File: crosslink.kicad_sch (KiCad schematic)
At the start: 1 part

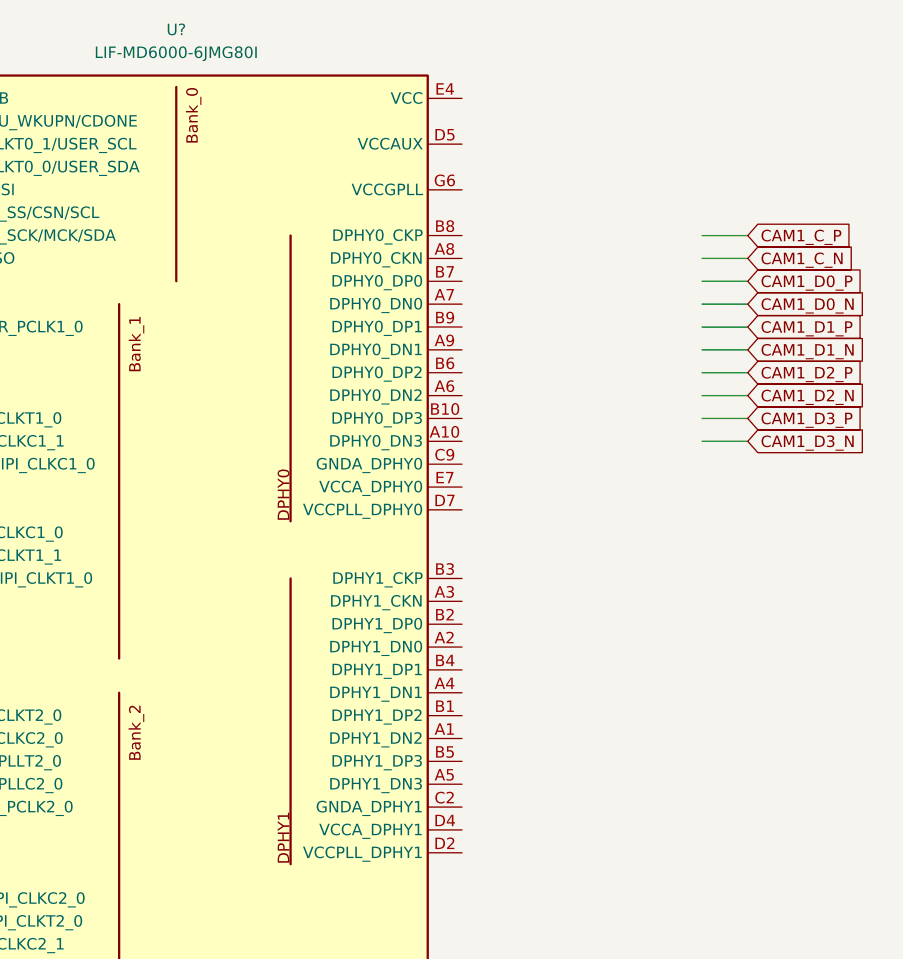
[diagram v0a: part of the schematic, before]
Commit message: [#52579] Connect CSI and DSI to CrossLink
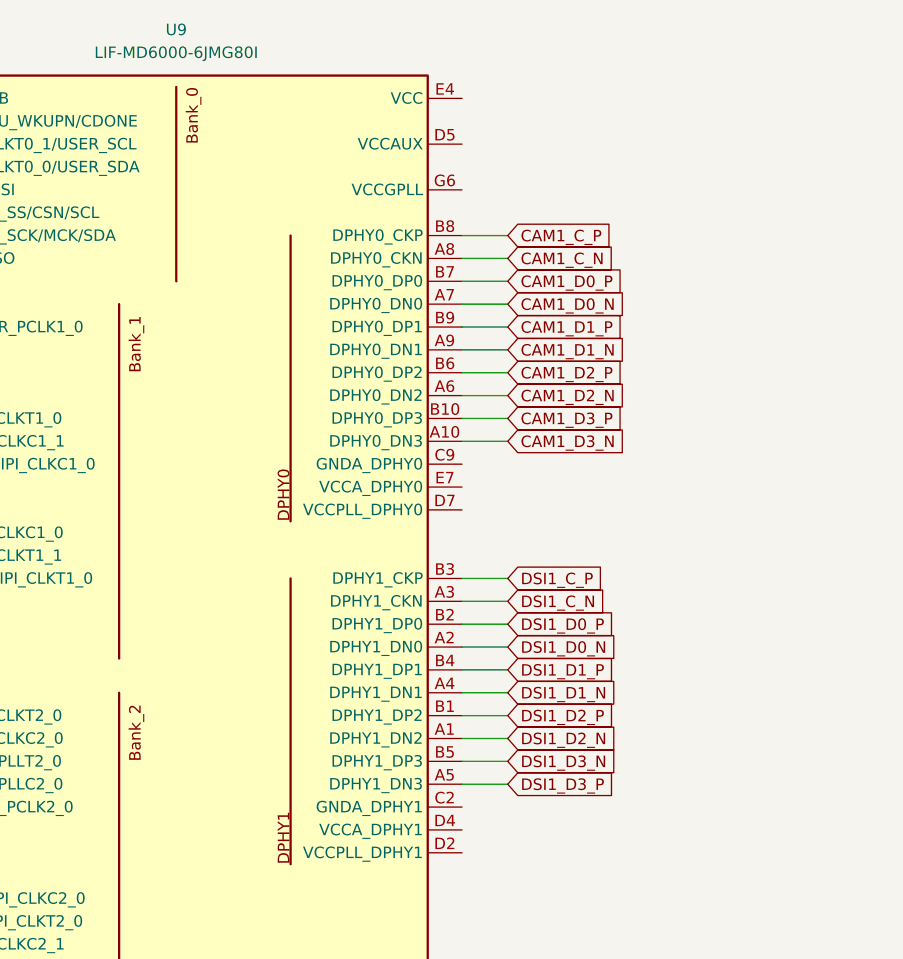
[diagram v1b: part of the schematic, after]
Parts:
- gave numbers to parts that had none: 1
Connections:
- net CAM1_C_N: now also U9.A8 (DPHY0_CKN)
- net CAM1_C_P: now also U9.B8 (DPHY0_CKP)
- net CAM1_D0_N: now also U9.A7 (DPHY0_DN0)
- net CAM1_D0_P: now also U9.B7 (DPHY0_DP0)
- net CAM1_D1_N: now also U9.A9 (DPHY0_DN1)
- net CAM1_D1_P: now also U9.B9 (DPHY0_DP1)
- net CAM1_D2_N: now also U9.A6 (DPHY0_DN2)
- net CAM1_D2_P: now also U9.B6 (DPHY0_DP2)
- net CAM1_D3_N: now also U9.A10 (DPHY0_DN3)
- net CAM1_D3_P: now also U9.B10 (DPHY0_DP3)
- net DSI1_D2_N: now reaches U9.A1 (DPHY1_DN2)
- net DSI1_D0_N: now reaches U9.A2 (DPHY1_DN0)
- net DSI1_C_N: now reaches U9.A3 (DPHY1_CKN)
- net DSI1_D1_N: now reaches U9.A4 (DPHY1_DN1)
- net DSI1_D3_P: now reaches U9.A5 (DPHY1_DN3)
- net DSI1_D2_P: now reaches U9.B1 (DPHY1_DP2)
- net DSI1_D0_P: now reaches U9.B2 (DPHY1_DP0)
- net DSI1_C_P: now reaches U9.B3 (DPHY1_CKP)
- net DSI1_D1_P: now reaches U9.B4 (DPHY1_DP1)
- net DSI1_D3_N: now reaches U9.B5 (DPHY1_DP3)

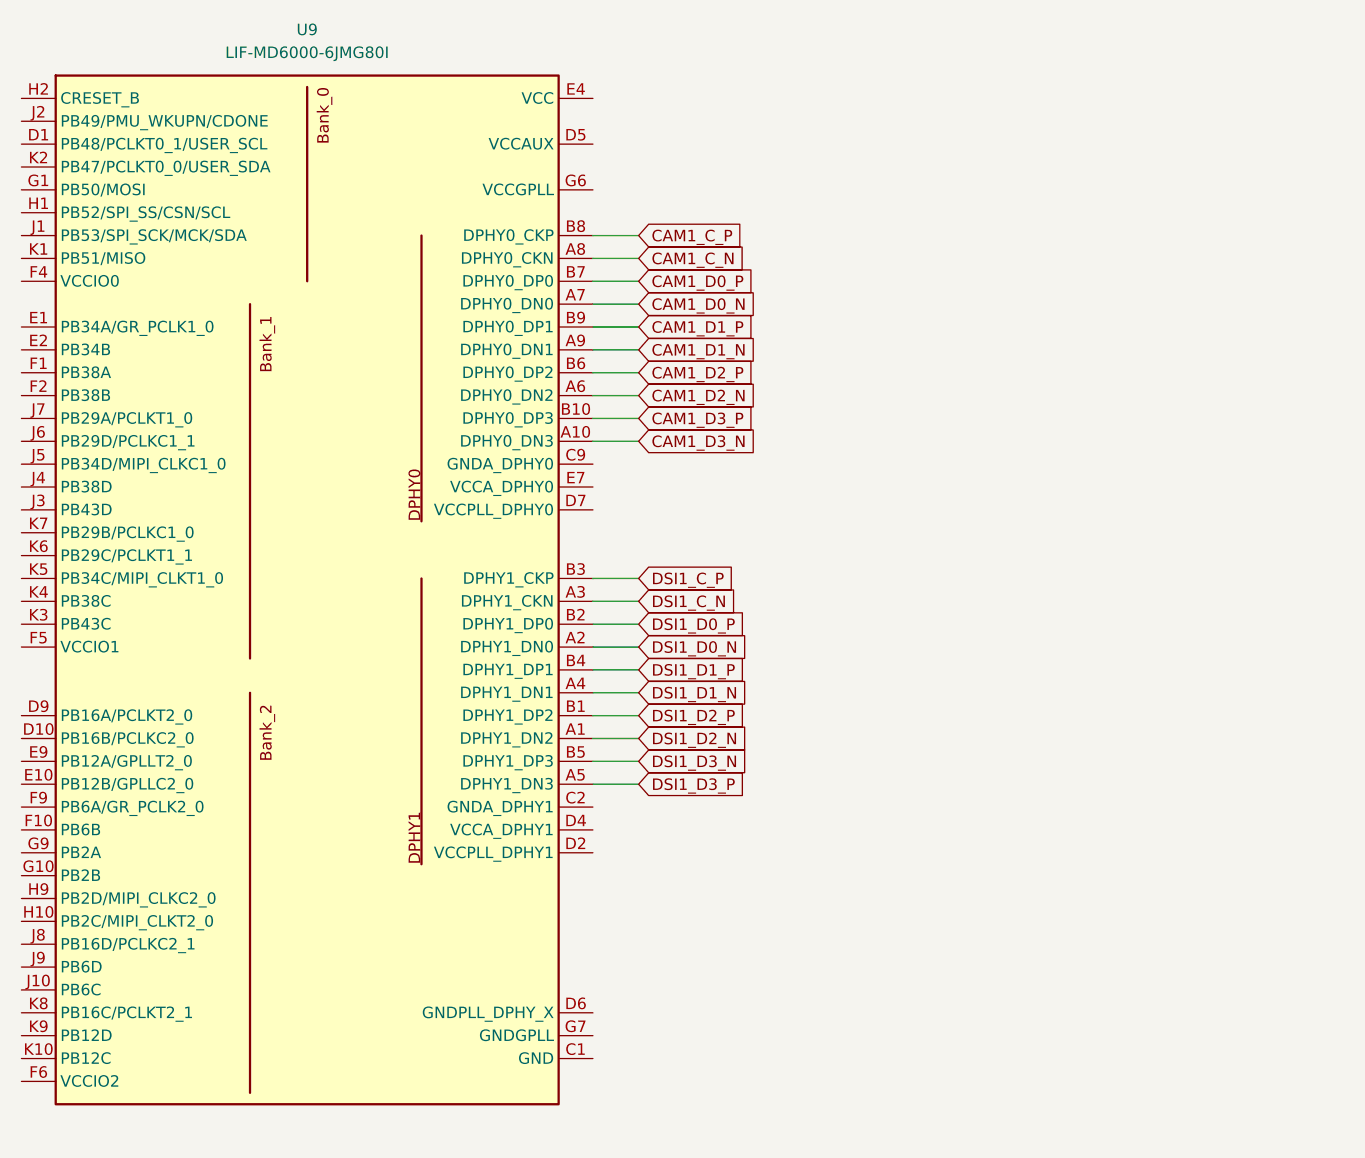
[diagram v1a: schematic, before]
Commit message: [#53847] Connect PF SoC to CrossLink
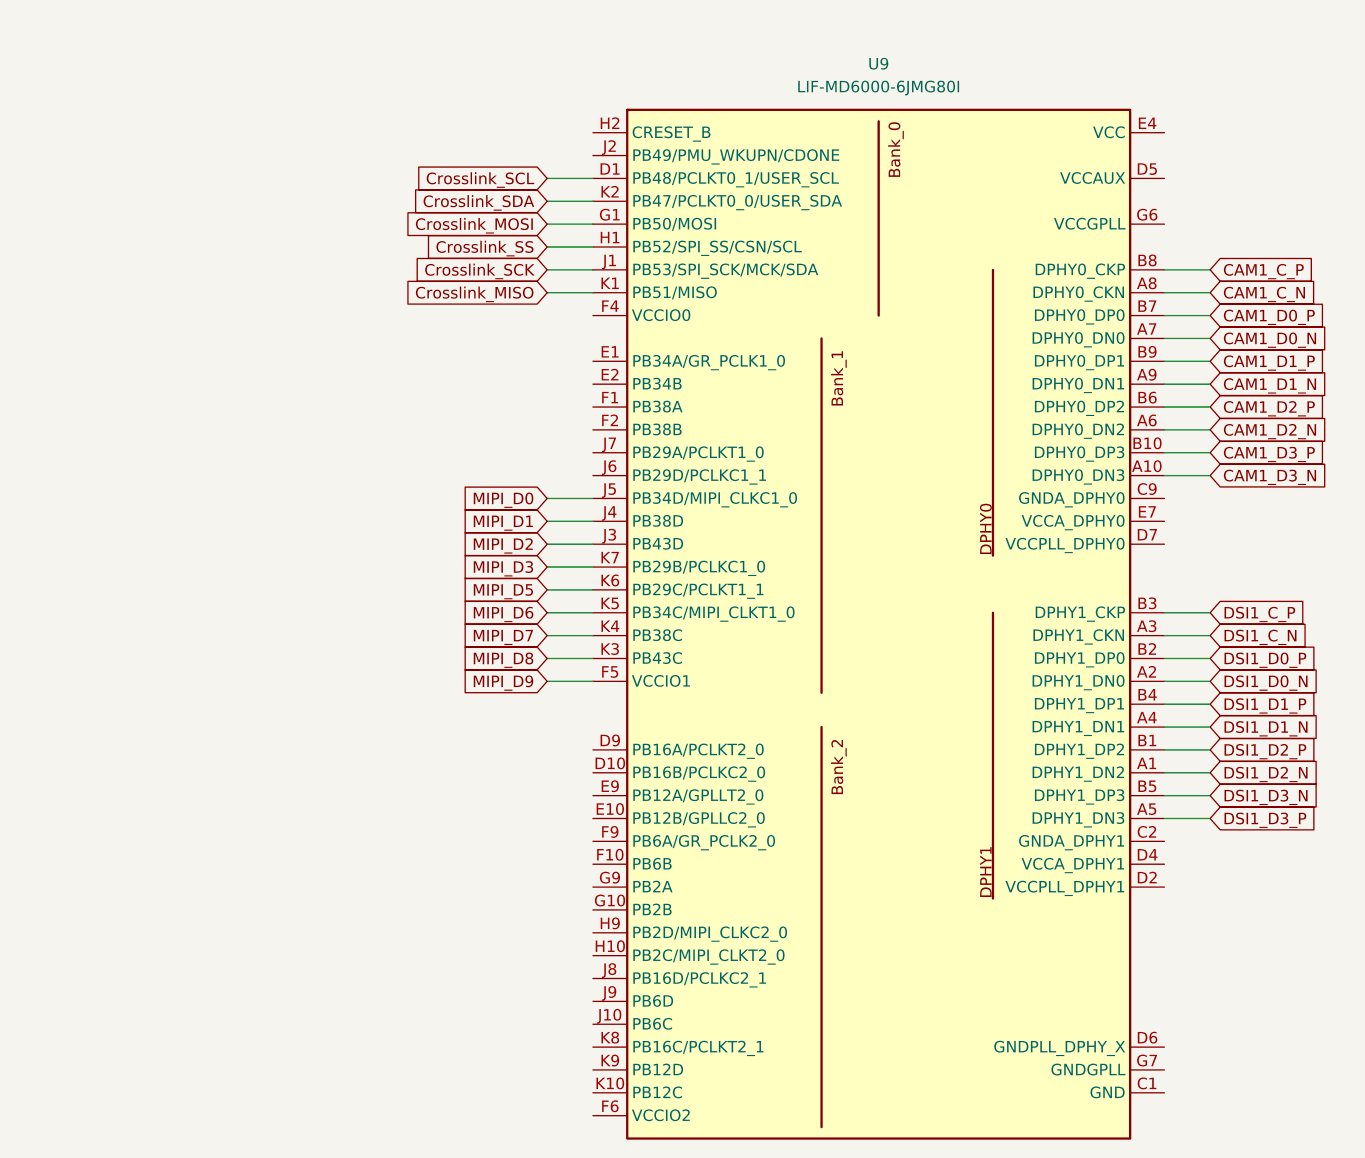
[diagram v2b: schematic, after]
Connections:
- net Crosslink_SCL: now reaches U9.D1 (PB48/PCLKT0_1/USER_SCL)
- net MIPI_D9: now reaches U9.F5 (VCCIO1), U9.G4 (VCCIO1)
- net Crosslink_MOSI: now reaches U9.G1 (PB50/MOSI)
- net Crosslink_SS: now reaches U9.H1 (PB52/SPI_SS/CSN/SCL)
- net Crosslink_SCK: now reaches U9.J1 (PB53/SPI_SCK/MCK/SDA)
- net MIPI_D2: now reaches U9.J3 (PB43D)
- net MIPI_D1: now reaches U9.J4 (PB38D)
- net MIPI_D0: now reaches U9.J5 (PB34D/MIPI_CLKC1_0)
- net Crosslink_MISO: now reaches U9.K1 (PB51/MISO)
- net Crosslink_SDA: now reaches U9.K2 (PB47/PCLKT0_0/USER_SDA)
- net MIPI_D8: now reaches U9.K3 (PB43C)
- net MIPI_D7: now reaches U9.K4 (PB38C)
- net MIPI_D6: now reaches U9.K5 (PB34C/MIPI_CLKT1_0)
- net MIPI_D5: now reaches U9.K6 (PB29C/PCLKT1_1)
- net MIPI_D3: now reaches U9.K7 (PB29B/PCLKC1_0)
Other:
- moved on the sheet: U9

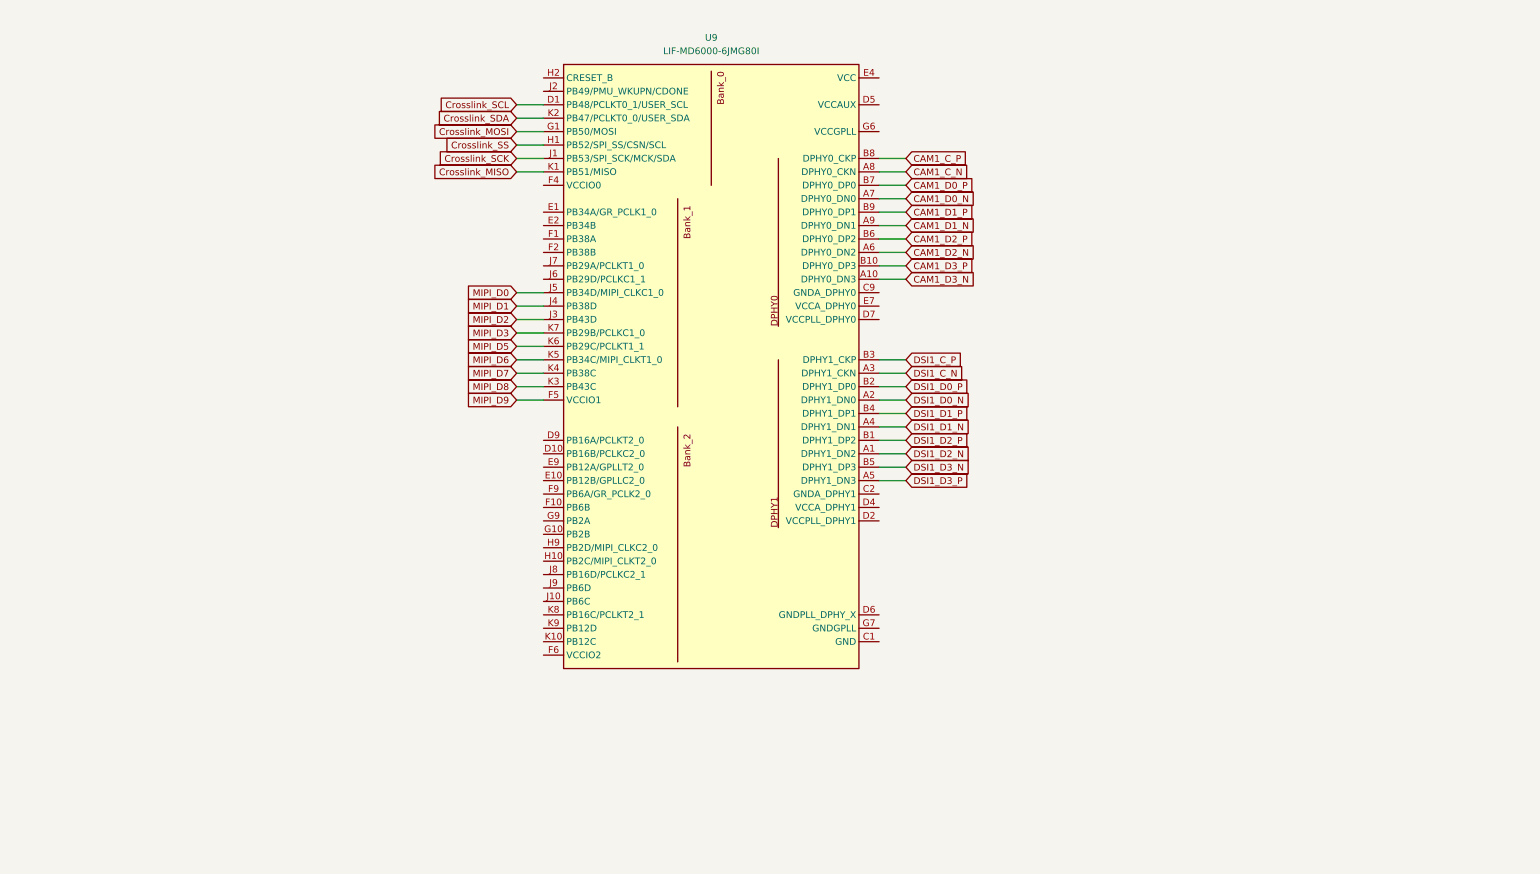
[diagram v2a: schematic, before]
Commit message: [#53847] Add PCLK to Crosslink data transmission
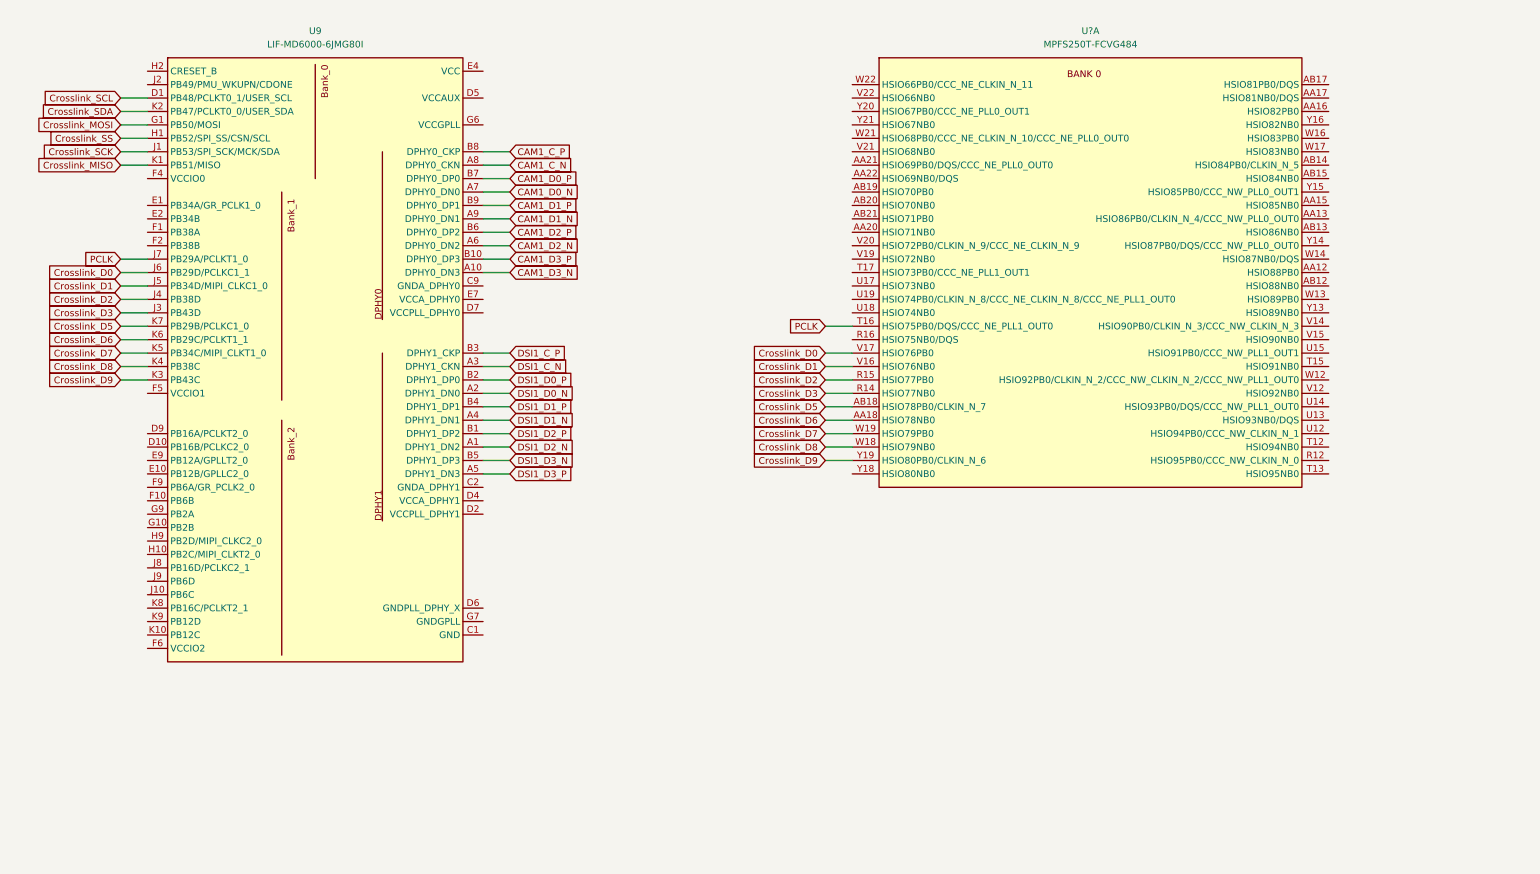
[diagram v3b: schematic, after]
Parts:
- added U?: MPFS250T-FCVG484, antmicro-footprints:BGA-484_19x19mm_Layout22x22_P0.8mm_FCVG484, symbol antmicroMicrocontrollers:MPFS250T-FCVG484
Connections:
- net Crosslink_D0: now reaches U9.J6 (PB29D/PCLKC1_1)
- net Crosslink_D0: now also U?.V17 (HSIO76PB0)
- net PCLK: now reaches U9.J7 (PB29A/PCLKT1_0)
- net PCLK: now also U?.T16 (HSIO75PB0/DQS/CCC_NE_PLL1_OUT0)
- net MIPI_D0 renamed Crosslink_D1
- net Crosslink_D1: now also U?.V16 (HSIO76NB0)
- net MIPI_D1 renamed Crosslink_D2
- net Crosslink_D2: now also U?.R15 (HSIO77PB0)
- net MIPI_D2 renamed Crosslink_D3
- net Crosslink_D3: now also U?.R14 (HSIO77NB0)
- net MIPI_D3 renamed Crosslink_D5
- net Crosslink_D5: now also U?.AB18 (HSIO78PB0/CLKIN_N_7)
- net MIPI_D5 renamed Crosslink_D6
- net Crosslink_D6: now also U?.AA18 (HSIO78NB0)
- net MIPI_D6 renamed Crosslink_D7
- net Crosslink_D7: now also U?.W19 (HSIO79PB0)
- net MIPI_D7 renamed Crosslink_D8
- net Crosslink_D8: now also U?.W18 (HSIO79NB0)
- net MIPI_D8 renamed Crosslink_D9
- net Crosslink_D9: now also U?.Y19 (HSIO80PB0/CLKIN_N_6)
- net MIPI_D9: no longer names the net of U9.F5 (VCCIO1), U9.G4 (VCCIO1)
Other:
- moved on the sheet: U9
